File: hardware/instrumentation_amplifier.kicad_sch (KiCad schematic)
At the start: 47 parts, among them U10 MCP6001-OT, U3 MCP6N11-010, U4 MCP4542, U9 MCP6001-OT

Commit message: Added net classes
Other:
- moved on the sheet: R45
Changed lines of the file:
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@@
 	(wire
 		(pts
-			(xy 142.24 134.62) (xy 146.05 134.62)
+			(xy 142.24 134.62) (xy 144.78 134.62)
 		)
 		(stroke
@@
 	(wire
 		(pts
-			(xy 153.67 134.62) (xy 154.94 134.62)
+			(xy 152.4 134.62) (xy 154.94 134.62)
 		)
 		(stroke
@@
 		)
 	)
+	(netclass_flag ""
+		(length 2.54)
+		(shape round)
+		(at 153.67 107.95 270)
+		(fields_autoplaced yes)
+		(effects
+			(font
+				(size 1.27 1.27)
+			)
+			(justify right bottom)
+		)
+		(property "Netclass" "Analog"
+			(at 156.21 107.2515 90)
+			(effects
+				(font
+					(size 1.27 1.27)
+				)
+				(justify left)
+			)
+		)
+		(property "Component Class" ""
+			(at -58.42 -2.54 0)
+			(effects
+				(font
+					(size 1.27 1.27)
+					(italic yes)
+				)
+			)
+		)
+	)
+	(netclass_flag ""
+		(length 2.54)
+		(shape round)
+		(at 237.49 40.64 0)
+		(fields_autoplaced yes)
+		(effects
+			(font
+				(size 1.27 1.27)
+			)
+			(justify left bottom)
+		)
+		(property "Netclass" "Analog"
+			(at 238.1885 38.1 0)
+			(effects
+				(font
+					(size 1.27 1.27)
+				)
+				(justify left)
+			)
+		)
+		(property "Component Class" ""
+			(at 25.4 -69.85 0)
+			(effects
+				(font
+					(size 1.27 1.27)
+					(italic yes)
+				)
+			)
+		)
+	)
+	(netclass_flag ""
+		(length 2.54)
+		(shape round)
+		(at 224.79 34.29 0)
+		(fields_autoplaced yes)
+		(effects
+			(font
+				(size 1.27 1.27)
+			)
+			(justify left bottom)
+		)
+		(property "Netclass" "Analog"
+			(at 225.4885 31.75 0)
+			(effects
+				(font
+					(size 1.27 1.27)
+				)
+				(justify left)
+			)
+		)
+		(property "Component Class" ""
+			(at 12.7 -76.2 0)
+			(effects
+				(font
+					(size 1.27 1.27)
+					(italic yes)
+				)
+			)
+		)
+	)
+	(netclass_flag ""
+		(length 2.54)
+		(shape round)
+		(at 153.67 134.62 180)
+		(fields_autoplaced yes)
+		(effects
+			(font
+				(size 1.27 1.27)
+			)
+			(justify right bottom)
+		)
+		(property "Netclass" "Analog"
+			(at 154.3685 137.16 0)
+			(effects
+				(font
+					(size 1.27 1.27)
+				)
+				(justify left)
+			)
+		)
+		(property "Component Class" ""
+			(at -58.42 24.13 0)
+			(effects
+				(font
+					(size 1.27 1.27)
+					(italic yes)
+				)
+			)
+		)
+	)
 	(symbol
 		(lib_id "Device:R")
@@
 	(symbol
 		(lib_id "Device:R")
-		(at 149.86 134.62 90)
+		(at 148.59 134.62 90)
 		(unit 1)
 		(exclude_from_sim no)
@@
 		(fields_autoplaced yes)
 		(property "Reference" "R45"
-			(at 149.86 128.27 90)
+			(at 148.59 128.27 90)
 			(effects
 				(font
@@
 		)
 		(property "Value" "1k 1%"
-			(at 149.86 130.81 90)
+			(at 148.59 130.81 90)
 			(effects
 				(font
@@
 		)
 		(property "Footprint" "Resistor_SMD:R_0603_1608Metric"
-			(at 149.86 136.398 90)
+			(at 148.59 136.398 90)
 			(effects
 				(font
@@
 		)
 		(property "Datasheet" "~"
-			(at 149.86 134.62 0)
+			(at 148.59 134.62 0)
 			(effects
 				(font
@@
 		)
 		(property "Description" "Resistor"
-			(at 149.86 134.62 0)
+			(at 148.59 134.62 0)
 			(effects
 				(font

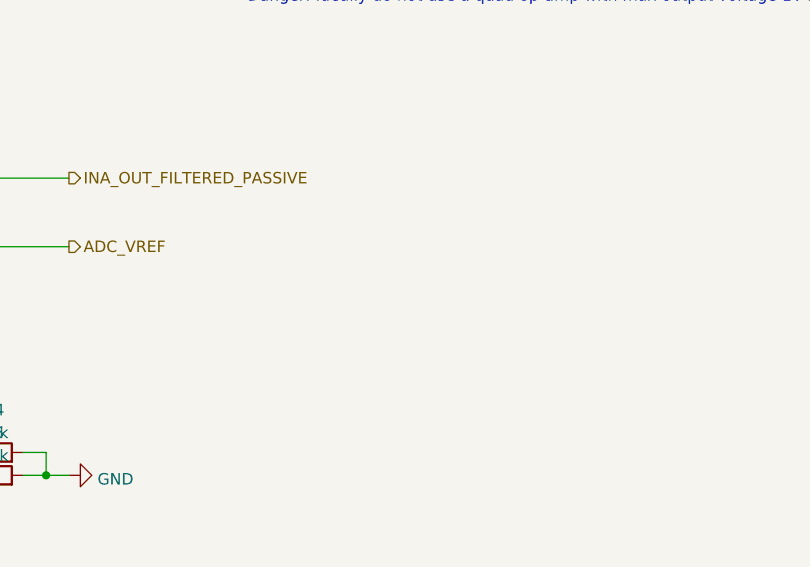
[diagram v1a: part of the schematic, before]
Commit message: Added note because of resistor availability
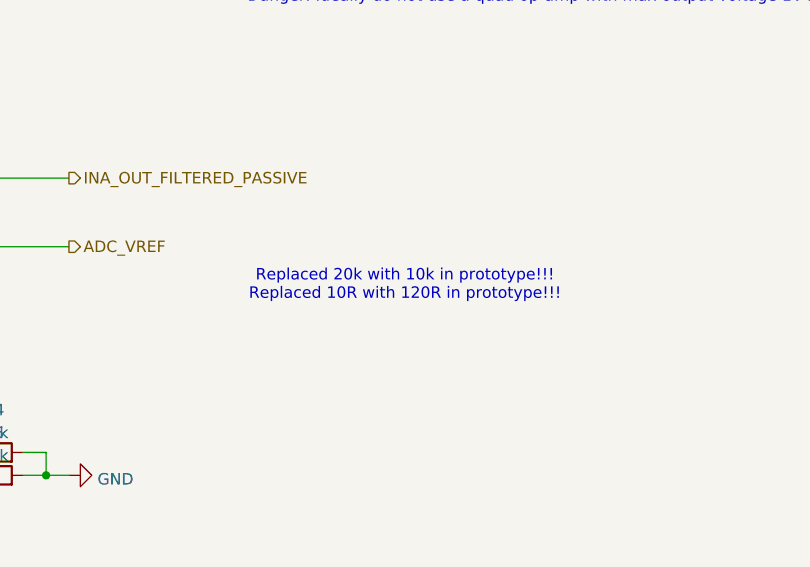
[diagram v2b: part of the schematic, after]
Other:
- note added: "Replaced 20k with 10k in prototype!!! Replaced 10R with 120R in prototype!!!"
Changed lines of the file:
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@@
+		)
+	)
+	(text "Replaced 20k with 10k in prototype!!!\nReplaced 10R with 120R in prototype!!!\n"
+		(exclude_from_sim no)
+		(at 235.458 107.188 0)
+		(effects
+			(font
+				(size 1.27 1.27)
+			)
 		)
 	)
